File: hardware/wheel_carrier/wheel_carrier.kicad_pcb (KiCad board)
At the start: 2 copper layers, 96 x 122 mm, 46 parts, among them J1 开发板左排 20P, J10 遥控·前差速, J11 遥控·后差速, J12 BEC 输入 6~7.4V, J13 扩展·左排(直连 J1), J14 扩展·右排(直连 J2), J15 电源排针, J16 电调·BEC输入, J17 接收机·油门, J2 开发板右排 20P, J3 霍尔·左前, J4 霍尔·右前, J5 霍尔·左后, J6 霍尔·右后, J7 舵机·前差速, J8 舵机·后差速, J9 遥控·模式, U1 LM2596T-5

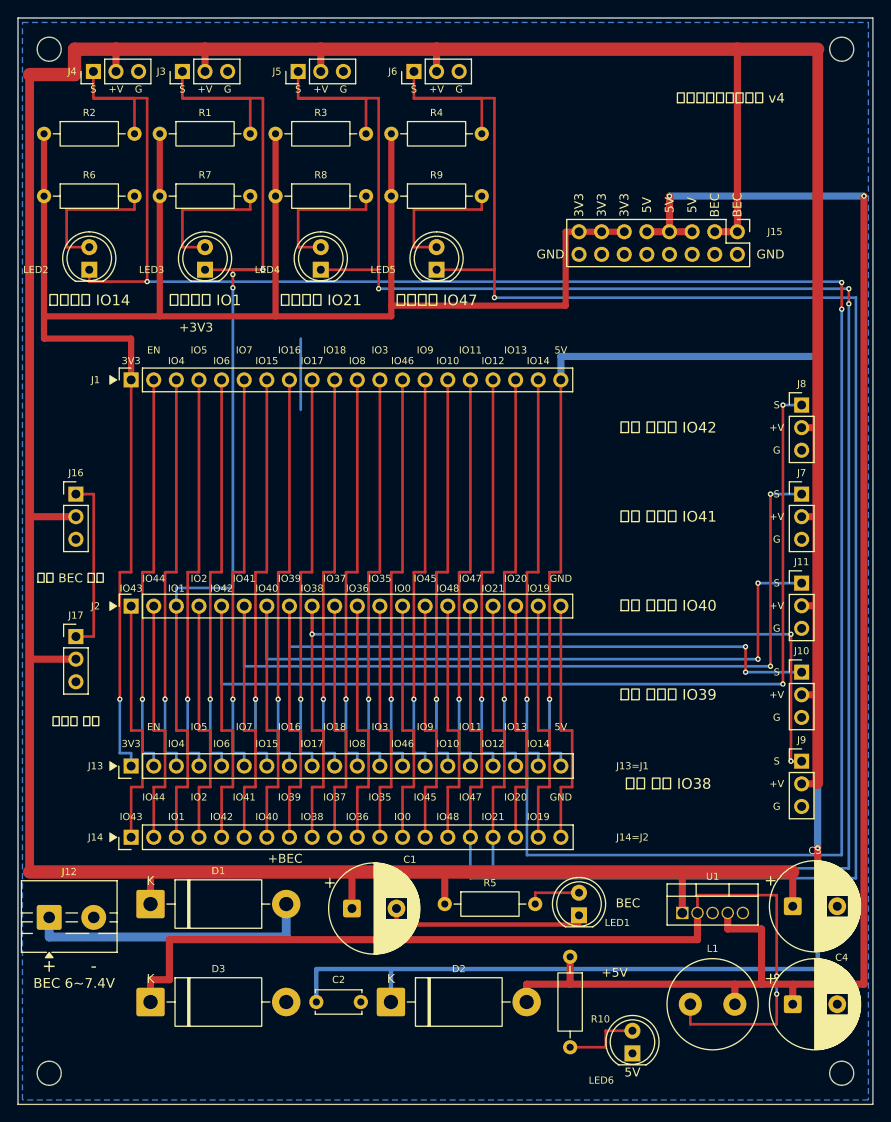
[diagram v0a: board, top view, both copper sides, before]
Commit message: feat(hw): v5 紧凑版——96×98.5，高度砍掉 19% 落进嘉立创免费档
目标是进嘉立创 100×100 的免费打样档，办法是只压 y 轴、x 轴一米不动
（宽度 96 本来就在档内），高度 122→98.5：

- J13/J14 从 J2 下方 18/26mm 收到 5.08mm（压缩的最大一笔）。扇形引出
  重写为"半间距错位车道"：J1 列的线走 x−1.27、J2 列走 x+1.27，两组
  按时段借用同一条物理车道，J1 的线在 y=60.5 打孔下 B 层直接扎进 J13
  ——40 针全在 F 层解完，过孔还从 47 个减到 40 个
- 右侧五路（舵机/遥控）改从 J14 的同网焊盘下方进入，不再穿 J13 行；
  霍尔四路改成"就近下车道、直达自己排针"的短路径（GPIO14 直接进
  J1.19、GPIO21/47 走东侧车道进 J2.17/16、GPIO1 下到 J2.3）
- 电源区重排：+5V 汇流提前到 y=84.6、开关节点与 DEV_5V 各自跳层让路、
  两个指示灯链跟着换位；v4 那根 GND 缝合线删了（空档已小到铺铜自己
  会忽略，留着反而是悬空端）
- 丝印全部重排：排针脚名从两行 0.8 号改成单行 0.58 号字，生成器自愈
  顺带把 .kicad_pro 的文字高度下限降到 0.55（与 lib_footprint_mismatch
  同一机制）；四个 1 脚三角标跟着新行位；板名升 v5
- 验证：DRC 0 违规 / 0 未连接 / 0 封装错误；丝印几何自检通过；钻带
  4×Ø2.7 安装孔在位；gerber/钻带/zip/预览图全部重导（前两者在
  .gitignore 里，磁盘上已更新）

Co-Authored-By: Claude Code <noreply@anthropic.com>
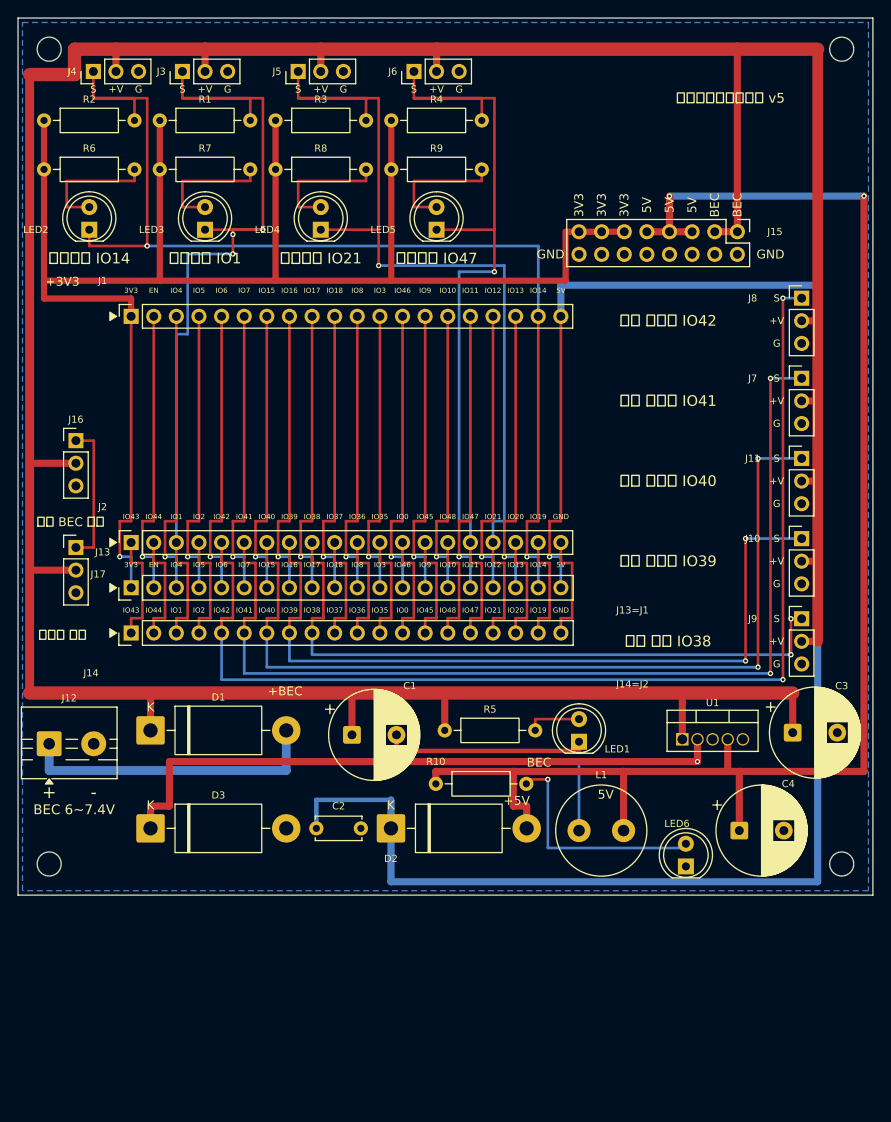
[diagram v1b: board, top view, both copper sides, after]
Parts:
- moved R10 24.6 mm to (46.9, 86.0), turned to 0 degrees
- moved ? 23.5 mm to (92.5, 95.0)
- moved ? 23.5 mm to (3.50, 95.0)
- moved L1 23.2 mm to (63.0, 91.2)
- moved J14 22.9 mm to (12.7, 69.1)
- moved LED6 21.8 mm to (75.0, 95.3)
- moved C4 20.4 mm to (81.0, 91.2)
- moved J13 20.0 mm to (12.7, 64.0)
- moved C1 19.5 mm to (37.5, 80.5)
- moved C2 19.5 mm to (33.5, 91.0)
- moved C3 19.5 mm to (87.0, 80.2)
- moved D1 19.5 mm to (14.9, 80.0)
- moved D2 19.5 mm to (41.9, 91.0)
- moved D3 19.5 mm to (14.9, 91.0)
- moved J12 19.5 mm to (3.50, 81.5)
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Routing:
- net GPIO14: track 281.1 -> 125.9 mm, vias 4 -> 2
- net GPIO47: track 234.8 -> 96.5 mm
- net GPIO21: track 241.4 -> 106.6 mm, vias 3 -> 1
- net +BEC: track 421.3 -> 388.2 mm
- net +3V3: track 218.3 -> 189.5 mm
- net GPIO38: track 100.9 -> 74.2 mm, vias 3 -> 2
- net GPIO1: track 125.4 -> 101.0 mm
- net GND: track 59.8 -> 36.0 mm
- net Net-(LED6-A): track 8.85 -> 26.6 mm, vias 0 -> 1
- net IO44: track 28.5 -> 12.7 mm
- net IO43: track 28.5 -> 12.7 mm
- net IO48: track 28.5 -> 12.7 mm
- net IO45: track 28.5 -> 12.7 mm
- net IO37: track 28.5 -> 12.7 mm
- net IO36: track 28.5 -> 12.7 mm
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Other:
- board size 96 x 122 mm -> 96 x 98.5 mm
- board text added: "轮速监测台转接底板 v5"
- board text removed: "轮速监测台转接底板 v4"

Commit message: feat(hw): 4S 输入升级 C1/R5/D3，补使用说明书
J12 端子可接 4S（≤16.8V）：C1 1000µF/25V、R5 1.5k、D3 SB560；原理图/PCB 器件值同步，封装和铜箔不变，接收机 +BEC 脚保持原样。

4S 时靠接线手动断开接收机/舵机 +V；README BOM 同步，新增 hardware/使用说明书.md。

Co-Authored-By: Claude Code <noreply@anthropic.com>
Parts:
- C1: value 1000µF/16V -> 1000µF/25V
- D3: value 1N5822 -> SB560
- R5: value 1k -> 1.5k
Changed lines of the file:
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@@
 			)
 		)
-		(property "Value" "1k"
+		(property "Value" "1.5k"
 			(at 5.08 2.37 0)
 			(layer "F.Fab")
@@
 			)
 		)
-		(property "Value" "1000µF/16V"
+		(property "Value" "1000µF/25V"
 			(at 2.5 6.25 0)
 			(layer "F.Fab")
@@
 			)
 		)
-		(property "Value" "1N5822"
+		(property "Value" "SB560"
 			(at 7.62 3.72 0)
 			(layer "F.Fab")

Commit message: feat(hw): v6 正面插装、舵机 5V、A3144 脚序，遥控三通道合并
- 开发板改为正面插装：J1 接右排 IO43 列，J2 接左排 3V3 列，针 1 仍在左端
- J7/J8 舵机 +V 改接板载 5V；J17 保持 BEC，接收机电源/地仍走 J17
- 霍尔 J3~J6 改为 +V/GND/信号，匹配 A3144 1=VCC、2=GND、3=OUT
- J10/J11 取消，遥控三通道合并为 J9 三针信号排针
- C4 升级 1000µF/16V，加强 5V 舵机瞬态
- 同步丝印、走线、脚序断言、README 与使用说明书；ERC/DRC 均 0/0

Co-Authored-By: Claude Code <noreply@anthropic.com>
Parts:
- removed J10: 遥控·前差速, Connector_PinHeader_2.54mm:PinHeader_1x03_P2.54mm_Vertical
- removed J11: 遥控·后差速, Connector_PinHeader_2.54mm:PinHeader_1x03_P2.54mm_Vertical
- C4: value 220µF/16V -> 1000µF/16V
- J1: value 开发板左排 20P -> 开发板排母1·右排(IO43列)
- J13: value 扩展·左排(直连 J1) -> 扩展·排母1(直连 J1/右排)
- J14: value 扩展·右排(直连 J2) -> 扩展·排母2(直连 J2/左排)
- J2: value 开发板右排 20P -> 开发板排母2·左排(3V3列)
- J9: value 遥控·模式 -> 遥控·三通道信号
- moved J9 18.0 mm to (88.0, 49.5)
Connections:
- J1 pad 1: +3V3 -> IO43
- J1 pad 10: IO18 -> IO37
- J1 pad 11: IO8 -> IO36
- J1 pad 12: IO3 -> IO35
- J1 pad 13: IO46 -> IO0
- J1 pad 14: IO9 -> IO45
- J1 pad 15: IO10 -> IO48
- J1 pad 16: IO11 -> GPIO47
- J1 pad 17: IO12 -> GPIO21
- J1 pad 18: IO13 -> IO20
- J1 pad 19: GPIO14 -> IO19
- J1 pad 2: EN -> IO44
- J1 pad 20: DEV_5V -> GND
- J1 pad 3: IO4 -> GPIO1
- J1 pad 4: IO5 -> IO2
- J1 pad 5: IO6 -> GPIO42
- J1 pad 6: IO7 -> GPIO41
- J1 pad 7: IO15 -> GPIO40
- J1 pad 8: IO16 -> GPIO39
- J1 pad 9: IO17 -> GPIO38
- J13 pad 1: +3V3 -> IO43
- J13 pad 10: IO18 -> IO37
- J13 pad 11: IO8 -> IO36
- J13 pad 12: IO3 -> IO35
- J13 pad 13: IO46 -> IO0
- J13 pad 14: IO9 -> IO45
- J13 pad 15: IO10 -> IO48
- J13 pad 16: IO11 -> GPIO47
- J13 pad 17: IO12 -> GPIO21
- J13 pad 18: IO13 -> IO20
- J13 pad 19: GPIO14 -> IO19
- J13 pad 2: EN -> IO44
- J13 pad 20: DEV_5V -> GND
- J13 pad 3: IO4 -> GPIO1
- J13 pad 4: IO5 -> IO2
- J13 pad 5: IO6 -> GPIO42
- J13 pad 6: IO7 -> GPIO41
- J13 pad 7: IO15 -> GPIO40
- J13 pad 8: IO16 -> GPIO39
- J13 pad 9: IO17 -> GPIO38
- J14 pad 1: IO43 -> +3V3
- J14 pad 10: IO37 -> IO18
- J14 pad 11: IO36 -> IO8
- J14 pad 12: IO35 -> IO3
- J14 pad 13: IO0 -> IO46
- J14 pad 14: IO45 -> IO9
- J14 pad 15: IO48 -> IO10
- J14 pad 16: GPIO47 -> IO11
- J14 pad 17: GPIO21 -> IO12
- J14 pad 18: IO20 -> IO13
- J14 pad 19: IO19 -> GPIO14
- J14 pad 2: IO44 -> EN
- J14 pad 20: GND -> DEV_5V
- J14 pad 3: GPIO1 -> IO4
- J14 pad 4: IO2 -> IO5
- J14 pad 5: GPIO42 -> IO6
- J14 pad 6: GPIO41 -> IO7
- J14 pad 7: GPIO40 -> IO15
- J14 pad 8: GPIO39 -> IO16
- J14 pad 9: GPIO38 -> IO17
- J2 pad 1: IO43 -> +3V3
- J2 pad 10: IO37 -> IO18
- J2 pad 11: IO36 -> IO8
- J2 pad 12: IO35 -> IO3
- J2 pad 13: IO0 -> IO46
- J2 pad 14: IO45 -> IO9
- J2 pad 15: IO48 -> IO10
- J2 pad 16: GPIO47 -> IO11
- J2 pad 17: GPIO21 -> IO12
- J2 pad 18: IO20 -> IO13
- J2 pad 19: IO19 -> GPIO14
- J2 pad 2: IO44 -> EN
- J2 pad 20: GND -> DEV_5V
- J2 pad 3: GPIO1 -> IO4
- J2 pad 4: IO2 -> IO5
- J2 pad 5: GPIO42 -> IO6
- J2 pad 6: GPIO41 -> IO7
- J2 pad 7: GPIO40 -> IO15
- J2 pad 8: GPIO39 -> IO16
- J2 pad 9: GPIO38 -> IO17
- J3 pad 1: GPIO1 -> +BEC
- J3 pad 2: +BEC -> GND
- J3 pad 3: GND -> GPIO1
- J4 pad 1: GPIO14 -> +BEC
- J4 pad 2: +BEC -> GND
- J4 pad 3: GND -> GPIO14
- J5 pad 1: GPIO21 -> +BEC
- J5 pad 2: +BEC -> GND
- J5 pad 3: GND -> GPIO21
- J6 pad 1: GPIO47 -> +BEC
- J6 pad 2: +BEC -> GND
- J6 pad 3: GND -> GPIO47
- J7 pad 2: +BEC -> +5V
- J8 pad 2: +BEC -> +5V
- J9 pad 2: +BEC -> GPIO39
- J9 pad 3: GND -> GPIO40
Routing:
- net +BEC: track 388.2 -> 303.7 mm
- net +5V: track 169.8 -> 226.4 mm
- net DEV_5V: track 204.3 -> 151.5 mm, vias 1 -> 0
- net GPIO38: track 74.2 -> 104.0 mm, vias 2 -> 3
- net GPIO39: track 87.1 -> 109.0 mm, vias 2 -> 3
- net IO8: track 33.0 -> 12.7 mm, vias 1 -> 0
- net IO37: track 12.7 -> 33.0 mm, vias 0 -> 1
- net IO36: track 12.7 -> 33.0 mm, vias 0 -> 1
- net IO35: track 12.7 -> 33.0 mm, vias 0 -> 1
- net IO3: track 33.0 -> 12.7 mm, vias 1 -> 0
- net IO20: track 12.7 -> 33.0 mm, vias 0 -> 1
- net IO19: track 12.7 -> 33.0 mm, vias 0 -> 1
- net IO18: track 33.0 -> 12.7 mm, vias 1 -> 0
- net IO17: track 33.0 -> 12.7 mm, vias 1 -> 0
- net IO13: track 33.0 -> 12.7 mm, vias 1 -> 0
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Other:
- board text added: "前"
- board text added: "后"
- board text added: "模"
- board text added: "正面插入 USB→"
- board text added: "轮速监测台转接底板 v6"
- board text added: "遥控 三通道"
- board text removed: "轮速监测台转接底板 v5"
- board text removed: "遥控 前差速 IO39"
- board text removed: "遥控 后差速 IO40"
- board text removed: "遥控 模式 IO38"

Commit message: fix(hw): J12 下移、取消左下角安装孔
- J12 端子下移，本体底边离板底约 6mm，给底部接线留出操作空间
- 取消左下角 M2.5 安装孔，安装孔从 4 个减到 3 个
- 重排 J12 到 D1 的输入走线与底部丝印（+/-、BEC 电压标注移到端子下方）
- README 补充 LED3 附近 B.Cu 空区的解释：GPIO1/GPIO14 横巷围成的孤立铜岛被 KiCad 删除

ERC 0/0，DRC 0/0；Gerber/钻孔与正反面预览已重出。

Co-Authored-By: Claude Code <noreply@anthropic.com>
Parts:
- removed the ? at (92.5, 95.0)
- moved ? 89.0 mm to (92.5, 95.0)
- moved J12 7.08 mm to (3.50, 88.6)
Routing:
- net Net-(D1-A): track 34.1 -> 35.2 mm
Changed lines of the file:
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@@
 	(footprint "TerminalBlock:TerminalBlock_MaiXu_MX126-5.0-02P_1x02_P5.00mm"
 		(layer "F.Cu")
-		(at 3.5 81.5)
+		(at 3.5 88.58)
 		(descr "terminal block MaiXu MX126-5.0-02P, 2 pins, pitch 5mm, size 10.5x7.8mm, drill diameter 1.3mm, pad diameter 2.8mm, https://www.lcsc.com/datasheet/lcsc_datasheet_2309150913_MAX-MX126-5-0-03P-GN01-Cu-S-A_C5188435.pdf")
 		(tags "THT terminal block MaiXu MX126-5.0-02P pitch 5mm size 10.5x7.8mm drill 1.3mm pad 2.8mm")
@@
 		)
 	)
-	(footprint "MountingHole:MountingHole_2.7mm_M2.5"
-		(layer "F.Cu")
-		(at 92.5 95)
-		(descr "Mounting Hole 2.7mm, M2.5, no annular, generated by kicad-footprint-generator mountinghole.py")
-		(tags "mountinghole M2.5")
-		(property "Reference" ""
-			(at 0 0 0)
-			(layer "F.SilkS")
-			(effects
-				(font
-					(size 1.27 1.27)
-				)
-			)
-		)
-		(property "Value" ""
-			(at 0 0 0)
-			(layer "F.Fab")
-			(effects
-				(font
-					(size 1.27 1.27)
-				)
-			)
-		)
-		(property "Datasheet" ""
-			(at 0 0 0)
-			(layer "F.Fab")
-			(hide yes)
-			(effects
-				(font
-					(size 1.27 1.27)
-				)
-			)
-		)
-		(property "Description" ""
-			(at 0 0 0)
-			(layer "F.Fab")
-			(hide yes)
-			(effects
-				(font
-					(size 1.27 1.27)
-				)
-			)
-		)
-		(attr exclude_from_pos_files exclude_from_bom)
-		(duplicate_pad_numbers_are_jumpers no)
-		(fp_circle
-			(center 0 0)
-			(end 2.7 0)
-			(stroke
-				(width 0.15)
-				(type solid)
-			)
-			(fill no)
-			(layer "Cmts.User")
-		)
-		(fp_circle
-			(center 0 0)
-			(end 2.95 0)
-			(stroke
-				(width 0.05)
-				(type solid)
-			)
-			(fill no)
-			(layer "F.CrtYd")
-		)
-		(fp_text user "${REFERENCE}"
-			(at 0 0 0)
-			(layer "F.Fab")
-			(effects
-				(font
-					(size 1 1)
-					(thickness 0.15)
-				)
-			)
-		)
-		(pad "" np_thru_hole circle
-			(at 0 0)
-			(size 2.7 2.7)
-			(drill 2.7)
-			(layers "*.Cu" "*.Mask")
-		)
-		(embedded_fonts no)
-	)
 	(footprint "LED_THT:LED_D5.0mm"
 		(layer "F.Cu")
@@
 	(footprint "MountingHole:MountingHole_2.7mm_M2.5"
 		(layer "F.Cu")
-		(at 3.5 95)
+		(at 92.5 95)
 		(descr "Mounting Hole 2.7mm, M2.5, no annular, generated by kicad-footprint-generator mountinghole.py")
 		(tags "mountinghole M2.5")
@@
 	)
 	(gr_text "BEC 6~7.4V"
-		(at 6.3 88.9 0)
+		(at 6.3 96.3 0)
 		(layer "F.SilkS")
 		(effects
@@
 	)
 	(gr_text "+"
-		(at 3.5 86.95 0)
+		(at 3.5 94 0)
 		(layer "F.SilkS")
 		(effects
@@
 	)
 	(gr_text "-"
-		(at 8.5 86.95 0)
+		(at 8.5 94 0)
 		(layer "F.SilkS")
 		(effects
@@
 	)
 	(segment
-		(start 3.5 81.5)
+		(start 3.5 88.58)
 		(end 3.5 84.5)
 		(width 1)
